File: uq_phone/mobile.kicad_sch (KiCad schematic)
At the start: 31 parts, among them J3 20279-001E-03, J4 20279-001E-03, Q1 MMBT3904LP-7, Q2 MMBT3904LP-7, U4 RC7620_1104625

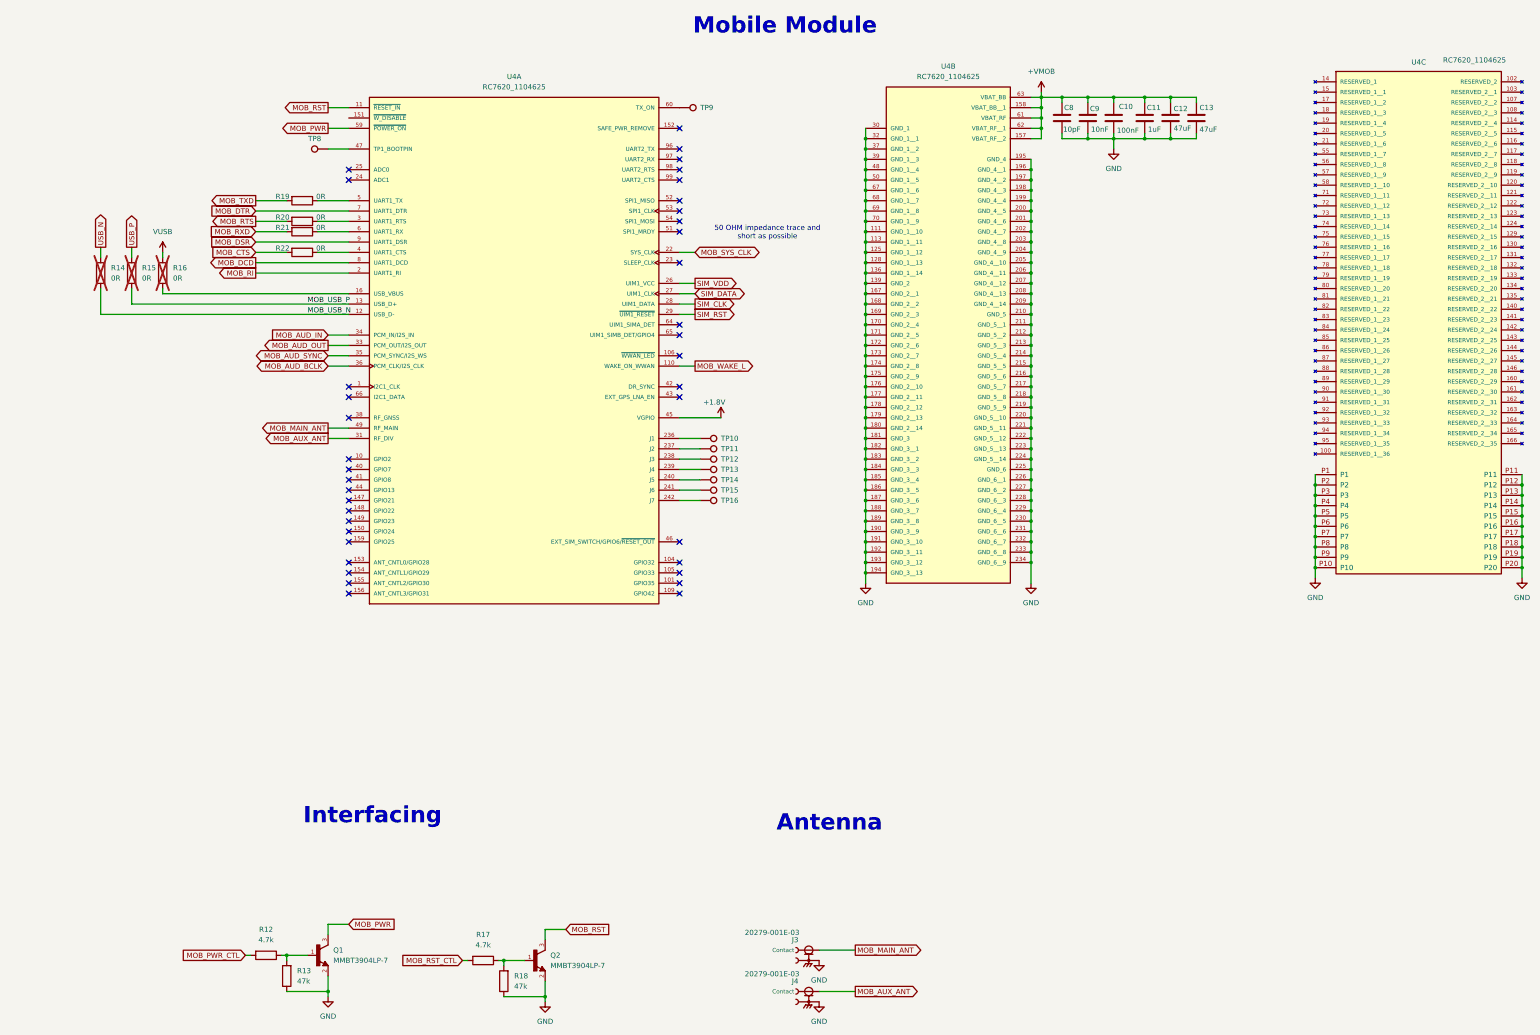
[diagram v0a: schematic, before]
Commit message: Swap RX TX
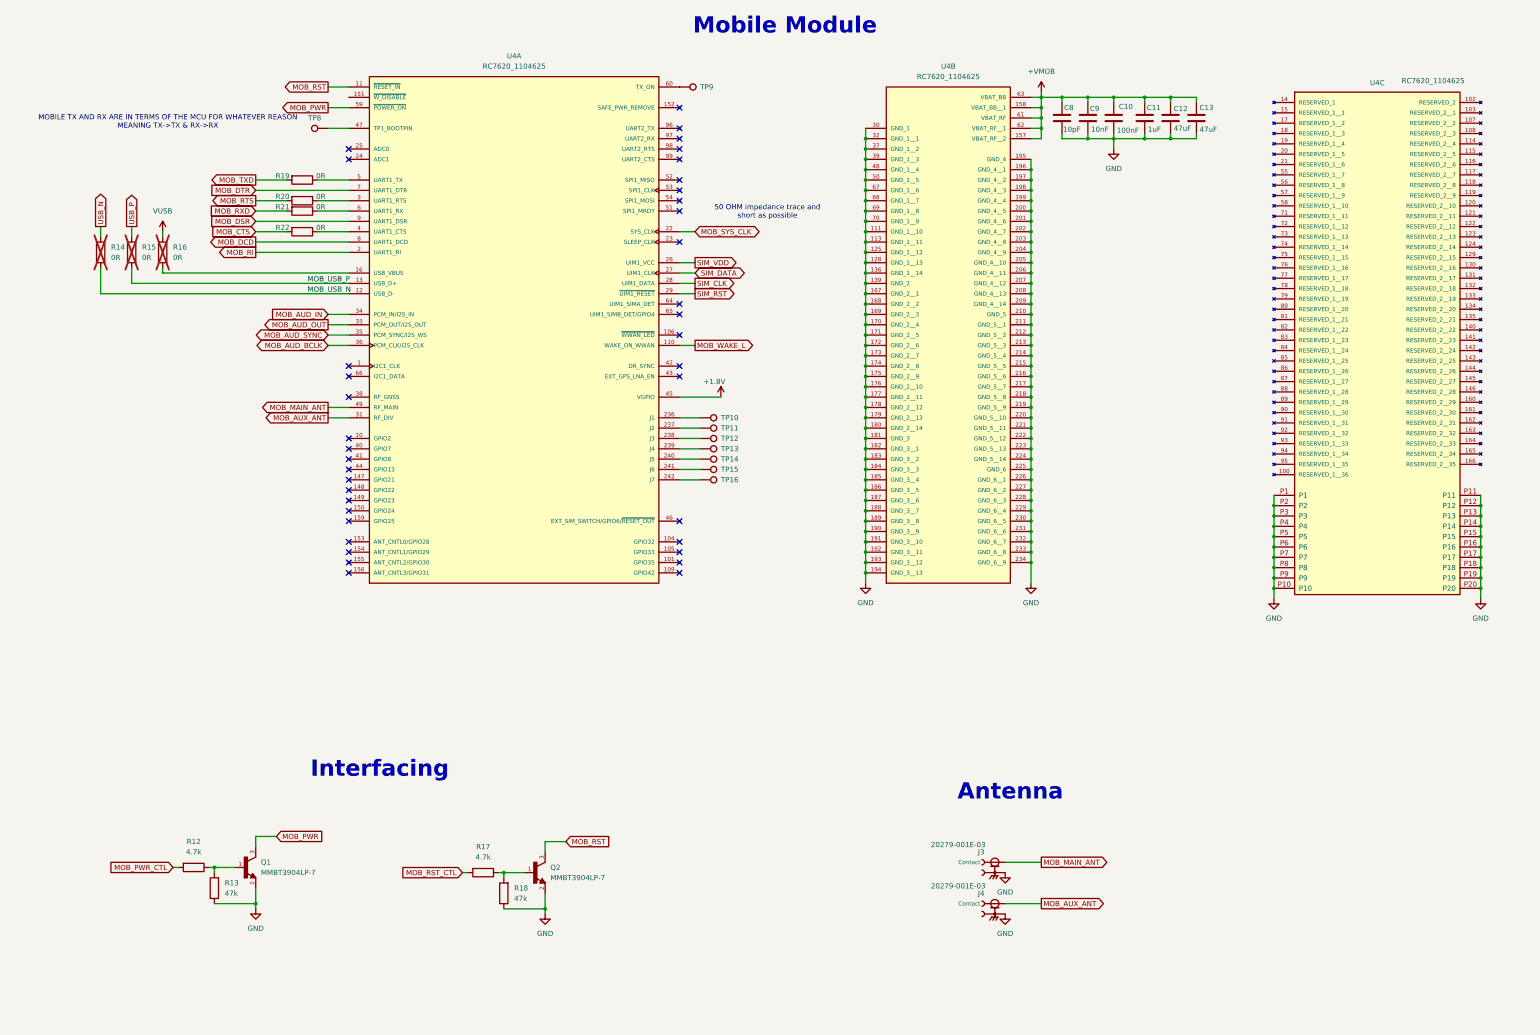
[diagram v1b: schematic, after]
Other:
- note added: "MOBILE TX AND RX ARE IN TERMS OF THE MCU FOR WHATEVER REASON MEANING TX->TX & RX->RX"
- moved on the sheet: J3, J4, Q1, Q2, R12, R13, R14, R15, R16, R17, R18, R19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

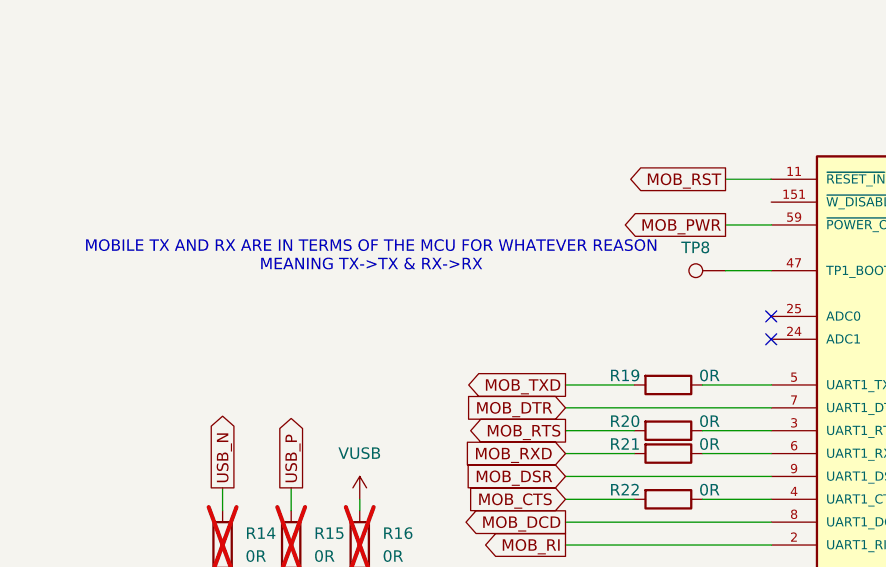
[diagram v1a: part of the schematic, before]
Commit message: Clean up and add DNP
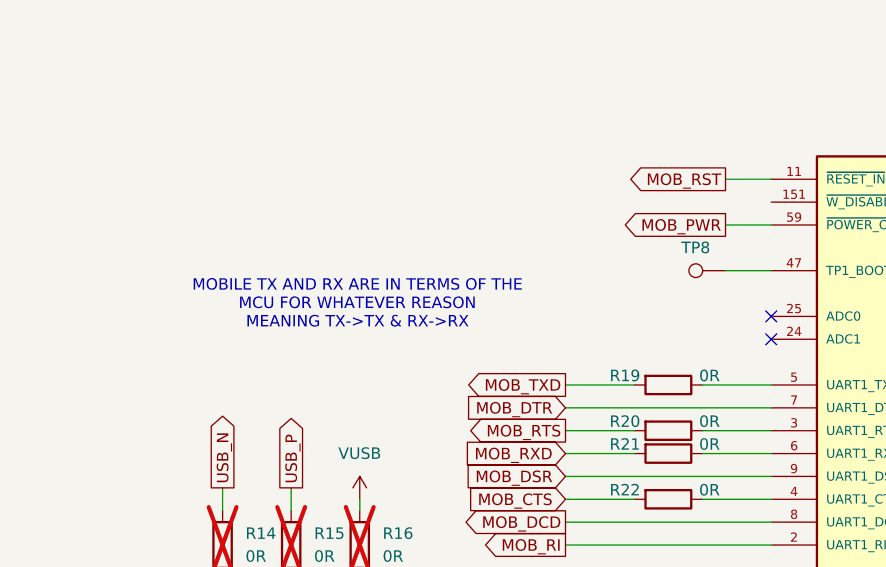
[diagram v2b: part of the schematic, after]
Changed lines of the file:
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@@
 		)
 	)
-	(text "MOBILE TX AND RX ARE IN TERMS OF THE MCU FOR WHATEVER REASON \nMEANING TX->TX & RX->RX"
+	(text "MOBILE TX AND RX ARE IN TERMS OF THE \nMCU FOR WHATEVER REASON \nMEANING TX->TX & RX->RX"
 		(exclude_from_sim no)
-		(at 38.1 44.196 0)
+		(at 36.576 49.53 0)
 		(effects
 			(font

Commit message: Minor changes
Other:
- note added: "Power Control"
- note removed: "Interfacing"
- moved on the sheet: J3, J4
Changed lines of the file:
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@@
 		(company "The University of Queensland")
 	)
-	(text "Interfacing\n"
+	(text "Power Control\n"
 		(exclude_from_sim no)
 		(at 90.17 203.2 0)
@@
 	(text "Antenna\n"
 		(exclude_from_sim no)
-		(at 245.11 208.788 0)
+		(at 292.1 206.248 0)
 		(effects
 			(font
@@
 	(wire
 		(pts
-			(xy 243.84 226.06) (xy 252.73 226.06)
+			(xy 290.83 223.52) (xy 299.72 223.52)
 		)
 		(stroke
@@
 	(wire
 		(pts
-			(xy 243.84 236.22) (xy 252.73 236.22)
+			(xy 290.83 233.68) (xy 299.72 233.68)
 		)
 		(stroke
@@
 	(global_label "MOB_MAIN_ANT"
 		(shape output)
-		(at 252.73 226.06 0)
+		(at 299.72 223.52 0)
 		(fields_autoplaced yes)
 		(effects
@@
 		)
 		(property "Intersheetrefs" "${INTERSHEET_REFS}"
-			(at 269.5643 226.06 0)
+			(at 316.5543 223.52 0)
 			(effects
 				(font
@@
 	)
 	(global_label "MOB_RTS"
-		(shape output)
+		(shape input)
 		(at 59.69 63.5 180)
 		(fields_autoplaced yes)
@@
 	(global_label "MOB_AUX_ANT"
 		(shape output)
-		(at 252.73 236.22 0)
+		(at 299.72 233.68 0)
 		(fields_autoplaced yes)
 		(effects
@@
 		)
 		(property "Intersheetrefs" "${INTERSHEET_REFS}"
-			(at 268.7176 236.22 0)
+			(at 315.7076 233.68 0)
 			(effects
 				(font
@@
 	)
 	(global_label "MOB_CTS"
-		(shape input)
+		(shape output)
 		(at 59.69 71.12 180)
 		(fields_autoplaced yes)
@@
 	(symbol
 		(lib_id "20279-001E-03:20279-001E-03")
-		(at 241.3 226.06 0)
+		(at 288.29 223.52 0)
 		(unit 1)
 		(exclude_from_sim no)
@@
 		(dnp no)
 		(property "Reference" "J3"
-			(at 238.76 223.52 0)
+			(at 285.75 220.98 0)
 			(effects
 				(font
@@
 		)
 		(property "Value" "20279-001E-03"
-			(at 239.014 221.742 0)
+			(at 286.004 219.202 0)
 			(effects
 				(font
@@
 		)
 		(property "Footprint" "20279-001E-03:IPEX_20279-001E-03"
-			(at 241.3 226.06 0)
+			(at 288.29 223.52 0)
 			(effects
 				(font
@@
 		)
 		(property "Datasheet" ""
-			(at 241.3 226.06 0)
+			(at 288.29 223.52 0)
 			(effects
 				(font
@@
 		)
 		(property "Description" ""
-			(at 241.3 226.06 0)
+			(at 288.29 223.52 0)
 			(effects
 				(font
@@
 		)
 		(property "MF" "I-PEX"
-			(at 241.3 226.06 0)
+			(at 288.29 223.52 0)
 			(effects
 				(font
@@
 		)
 		(property "MAXIMUM_PACKAGE_HEIGHT" "1.25mm"
-			(at 241.3 226.06 0)
+			(at 288.29 223.52 0)
 			(effects
 				(font
@@
 		)
 		(property "Package" "None"
-			(at 241.3 226.06 0)
+			(at 288.29 223.52 0)
 			(effects
 				(font
@@
 		)
 		(property "Price" "None"
-			(at 241.3 226.06 0)
+			(at 288.29 223.52 0)
 			(effects
 				(font
@@
 		)
 		(property "Check_prices" "https://www.snapeda.com/parts/20279-001E-03/I-PEX/view-part/?ref=eda"
-			(at 241.3 226.06 0)
+			(at 288.29 223.52 0)
 			(effects
 				(font
@@
 		)
 		(property "STANDARD" "Manufacturer Recommendations"
-			(at 241.3 226.06 0)
+			(at 288.29 223.52 0)
 			(effects
 				(font
@@
 		)
 		(property "PARTREV" "32"
-			(at 241.3 226.06 0)
+			(at 288.29 223.52 0)
 			(effects
 				(font
@@
 		)
 		(property "SnapEDA_Link" "https://www.snapeda.com/parts/20279-001E-03/I-PEX/view-part/?ref=snap"
-			(at 241.3 226.06 0)
+			(at 288.29 223.52 0)
 			(effects
 				(font
@@
 		)
 		(property "MP" "20279-001E-03"
-			(at 241.3 226.06 0)
+			(at 288.29 223.52 0)
 			(effects
 				(font
@@
 		)
 		(property "Description_1" "\n                        \n                            1 POS Vertical SMD Small form factor with big performance through 6 GHz connector,MHF, RF, micro-coaxial MHF I Receptacle\n                        \n"
-			(at 241.3 226.06 0)
+			(at 288.29 223.52 0)
 			(effects
 				(font
@@
 		)
 		(property "Availability" "In Stock"
-			(at 241.3 226.06 0)
+			(at 288.29 223.52 0)
 			(effects
 				(font
@@
 		)
 		(property "MANUFACTURER" "I-PEX"
-			(at 241.3 226.06 0)
+			(at 288.29 223.52 0)
 			(effects
 				(font
@@
 	(symbol
 		(lib_id "20279-001E-03:20279-001E-03")
-		(at 241.3 236.22 0)
+		(at 288.29 233.68 0)
 		(unit 1)
 		(exclude_from_sim no)
@@
 		(dnp no)
 		(property "Reference" "J4"
-			(at 238.76 233.68 0)
+			(at 285.75 231.14 0)
 			(effects
 				(font
@@
 		)
 		(property "Value" "20279-001E-03"
-			(at 239.014 231.902 0)
+			(at 286.004 229.362 0)
 			(effects
 				(font
@@
 		)
 		(property "Footprint" "20279-001E-03:IPEX_20279-001E-03"
-			(at 241.3 236.22 0)
+			(at 288.29 233.68 0)
 			(effects
 				(font
@@
 		)
 		(property "Datasheet" ""
-			(at 241.3 236.22 0)
+			(at 288.29 233.68 0)
 			(effects
 				(font
@@
 		)
 		(property "Description" ""
-			(at 241.3 236.22 0)
+			(at 288.29 233.68 0)
 			(effects
 				(font
@@
 		)
 		(property "MF" "I-PEX"
-			(at 241.3 236.22 0)
+			(at 288.29 233.68 0)
 			(effects
 				(font
@@
 		)
 		(property "MAXIMUM_PACKAGE_HEIGHT" "1.25mm"
-			(at 241.3 236.22 0)
+			(at 288.29 233.68 0)
 			(effects
 				(font
@@
 		)
 		(property "Package" "None"
-			(at 241.3 236.22 0)
+			(at 288.29 233.68 0)
 			(effects
 				(font
@@
 		)
 		(property "Price" "None"
-			(at 241.3 236.22 0)
+			(at 288.29 233.68 0)
 			(effects
 				(font
@@
 		)
 		(property "Check_prices" "https://www.snapeda.com/parts/20279-001E-03/I-PEX/view-part/?ref=eda"
-			(at 241.3 236.22 0)
+			(at 288.29 233.68 0)
 			(effects
 				(font
@@
 		)
 		(property "STANDARD" "Manufacturer Recommendations"
-			(at 241.3 236.22 0)
+			(at 288.29 233.68 0)
 			(effects
 				(font
@@
 		)
 		(property "PARTREV" "32"
-			(at 241.3 236.22 0)
+			(at 288.29 233.68 0)
 			(effects
 				(font
@@
 		)
 		(property "SnapEDA_Link" "https://www.snapeda.com/parts/20279-001E-03/I-PEX/view-part/?ref=snap"
-			(at 241.3 236.22 0)
+			(at 288.29 233.68 0)
 			(effects
 				(font
@@
 		)
 		(property "MP" "20279-001E-03"
-			(at 241.3 236.22 0)
+			(at 288.29 233.68 0)
 			(effects
 				(font
@@
 		)
 		(property "Description_1" "\n                        \n                            1 POS Vertical SMD Small form factor with big performance through 6 GHz connector,MHF, RF, micro-coaxial MHF I Receptacle\n                        \n"
-			(at 241.3 236.22 0)
+			(at 288.29 233.68 0)
 			(effects
 				(font
@@
 		)
 		(property "Availability" "In Stock"
-			(at 241.3 236.22 0)
+			(at 288.29 233.68 0)
 			(effects
 				(font
@@
 		)
 		(property "MANUFACTURER" "I-PEX"
-			(at 241.3 236.22 0)
+			(at 288.29 233.68 0)
 			(effects
 				(font
@@
 	(symbol
 		(lib_id "power:GND")
-		(at 243.84 228.6 0)
+		(at 290.83 226.06 0)
 		(unit 1)
 		(exclude_from_sim no)
@@
 		(dnp no)
 		(property "Reference" "#PWR036"
-			(at 243.84 234.95 0)
+			(at 290.83 232.41 0)
 			(effects
 				(font
@@
 		)
 		(property "Value" "GND"
-			(at 243.84 233.426 0)
+			(at 290.83 230.886 0)
 			(effects
 				(font
@@
 		)
 		(property "Footprint" ""
-			(at 243.84 228.6 0)
+			(at 290.83 226.06 0)
 			(effects
 				(font
@@
 		)
 		(property "Datasheet" ""
-			(at 243.84 228.6 0)
+			(at 290.83 226.06 0)
 			(effects
 				(font
@@
 		)
 		(property "Description" "Power symbol creates a global label with name \"GND\" , ground"
-			(at 243.84 228.6 0)
+			(at 290.83 226.06 0)
 			(effects
 				(font
@@
 	(symbol
 		(lib_id "power:GND")
-		(at 243.84 238.76 0)
+		(at 290.83 236.22 0)
 		(unit 1)
 		(exclude_from_sim no)
@@
 		(dnp no)
 		(property "Reference" "#PWR037"
-			(at 243.84 245.11 0)
+			(at 290.83 242.57 0)
 			(effects
 				(font
@@
 		)
 		(property "Value" "GND"
-			(at 243.84 243.586 0)
+			(at 290.83 241.046 0)
 			(effects
 				(font
@@
 		)
 		(property "Footprint" ""
-			(at 243.84 238.76 0)
+			(at 290.83 236.22 0)
 			(effects
 				(font
@@
 		)
 		(property "Datasheet" ""
-			(at 243.84 238.76 0)
+			(at 290.83 236.22 0)
 			(effects
 				(font
@@
 		)
 		(property "Description" "Power symbol creates a global label with name \"GND\" , ground"
-			(at 243.84 238.76 0)
+			(at 290.83 236.22 0)
 			(effects
 				(font

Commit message: Generate Early production outputs
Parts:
- C10: LCSC PN (none) -> C307331
- C11: LCSC PN (none) -> C52923
- C12, C13: LCSC PN (none) -> C109461
- C8: LCSC PN (none) -> C2168222
- C9: LCSC PN (none) -> C15195
- J3, J4: LCSC PN (none) -> C36499136
- Q1, Q2: Description_1 Bipolar (BJT) Transistor NPN 40 V 200 mA 300MHz 250 mW Surface Mount X1-DFN1006-3 -> Bipolar (BJT) Transistor NPN 40 V 200 mA 300MHz 250 mW Surface Mount X1-DFN1006-3; LCSC PN (none) -> C460099
- R12, R17: LCSC PN (none) -> C606173
- R13, R18: LCSC PN (none) -> C427250
- R14, R15, R16, R19, R20, R21, R22: LCSC PN (none) -> C95177
- U4: value RC7620_1104625 -> WP SNAP-IN BASE_6000636

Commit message: Fix outputs
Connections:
- no-connect marks 38 -> 39
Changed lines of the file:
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@@
+	)
+	(no_connect
+		(at 82.55 38.1)
 	)
 	(no_connect
